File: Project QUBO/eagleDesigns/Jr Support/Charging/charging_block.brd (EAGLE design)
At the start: 160 x 100 mm, 115 parts

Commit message: 
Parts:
- removed U$38: (no value), resistor:DRQ125-600
- added L1, L2: 10u, resistor:L6100
- added LED7, LED8: Green, led:CHIP-LED0805
- added R28, R33: 330, resistor:R0805
- moved U$21 217.5 mm to (141.0, 17.8), turned to 180 degrees
- moved LED6 212.1 mm to (114.3, 26.7)
- moved LED5 208.6 mm to (119.4, 26.7)
- moved LED4 207.3 mm to (124.5, 26.7)
- moved U$2 194.7 mm to (97.8, 54.0), turned to 180 degrees
- moved C12 187.0 mm to (87.6, 20.3)
- moved U$20 185.2 mm to (115.6, 90.2)
- moved R22 176.3 mm to (109.2, 24.1)
- moved U$5 175.7 mm to (95.2, 63.5)
- moved U$19 174.4 mm to (123.2, 90.2)
- moved R21 170.3 mm to (109.2, 27.9)
- moved D2 169.9 mm to (83.9, 52.9), turned to 270 degrees
- moved R18 166.0 mm to (118.1, 22.9)
- moved R16 165.1 mm to (125.7, 33.0)
- moved R20 164.3 mm to (109.2, 31.8)
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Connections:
- new net N$35: LED7.A, R28.1
- new net N$57: LED8.A, R33.1
- net GND: now also LED7.C, LED8.C
- net N$17: now also L2.P$1; no longer U$38.P$2
- net N$20: now also L2.P$2; no longer U$38.P$4
- net N$77: now also L1.P$2; no longer U$38.P$3
- net N$81: now also L1.P$1; no longer U$38.P$1
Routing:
- net GND: track 0.00 -> 2.36 mm, vias 0 -> 1

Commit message: Charging board layout, rev. 1
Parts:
- added R35, R36, R37: 0, resistor:R0805
- C19: value 100u,<50mO -> 120uF; device resistor:C0805 -> resistor:E3,5-8
- C84: value 100u,<50mO -> 120u; device resistor:C0805 -> resistor:E3,5-8
- R28: value 330 -> 1.5k
- moved V_OUT 96.4 mm to (87.0, 88.3)
- moved U$21 82.9 mm to (87.0, 80.6)
- moved U$19 74.3 mm to (49.5, 80.6), flipped to the bottom, turned to 270 degrees
- moved ON 71.5 mm to (56.5, 34.9)
- moved U$58 71.4 mm to (62.2, 36.2), turned to 90 degrees
- moved C60 66.8 mm to (62.9, 45.1)
- moved R23 60.0 mm to (62.9, 42.5), turned to 180 degrees
- moved R24 57.7 mm to (62.9, 40.0), turned to 180 degrees
- moved U$56 57.3 mm to (62.2, 48.9)
- moved U$57 55.7 mm to (56.5, 44.5), turned to 270 degrees
- moved U$20 54.7 mm to (61.0, 86.4), turned to 180 degrees
- moved C61 53.4 mm to (54.6, 40.0)
- moved C62 52.7 mm to (59.7, 40.0), turned to 270 degrees
- moved AUDIO 52.3 mm to (26.7, 89.5), turned to 180 degrees
- moved R14 47.3 mm to (29.2, 83.2), turned to 270 degrees
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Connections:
- net N$11 renamed BATT1_P
- net N$15 renamed DLO_2
- net N$16 renamed DHI_2
- net N$17 renamed L-IN_2
- net N$18 renamed PGND_2
- net N$20 renamed CS_2
- net N$21 renamed THM_2
- net N$42 renamed DCIN_2
- net N$43 renamed BATT2_P
- net N$45 renamed VIN
- net N$46 renamed FET-G_1
- net N$56 renamed FET-D_1
- net N$77 renamed CS_1
- removed net N$48: C60.2, ON.P$2, U$56.P$3, U$58.P$1
- removed net V_BATT1: C83.1, C84.1, R29.1, R34.1, U$17.P$2, U$33.7
- removed net V_BATT2: C18.1, C19.1, R5.1, R7.1, U$1.7, U$18.P$2
- new net BATT1_M: BATT1_CHARGE.P$2, R35.1, R37.1, U$15.P$1, U$40.P$2
- new net BATT2_M: BATT2_CHARGE.P$2, R36.2, U$13.P$1, U$6.P$2
- new net BATT_1: C83.1, C84.+, R29.1, R34.1, U$17.P$2, U$33.7
- new net BATT_2: C18.1, C19.+, R5.1, R7.1, U$1.7, U$18.P$2
- net !SHDN!: now also R33.2
- net GND: now also C19.-, C60.2, C84.-, ON.P$2, R35.2, R36.1, R37.2, U$56.P$3, U$58.P$1; no longer BATT1_CHARGE.P$2, BATT2_CHARGE.P$2, C19.2, C84.2, U$13.P$1, U$15.P$1, U$40.P$2, U$6.P$2
- net V_SHORE: now also R28.2
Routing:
- net V_SHORE: track 0.00 -> 241.1 mm, vias 0 -> 5
- net !SHDN!: track 0.00 -> 58.3 mm, vias 0 -> 4
- net BATT_2: track 0.00 -> 41.8 mm
- net N$31: track 0.00 -> 36.5 mm, vias 0 -> 2
- net N$27: track 0.00 -> 29.9 mm, vias 0 -> 2
- net THM_2: track 0.00 -> 27.8 mm, vias 0 -> 1
- net N$32: track 0.00 -> 27.2 mm, vias 0 -> 2
- net N$38: track 0.00 -> 25.5 mm, vias 0 -> 2
- net N$24: track 0.00 -> 23.7 mm, vias 0 -> 2
- net VIN: track 0.00 -> 23.7 mm
- net CS_1: track 0.00 -> 23.1 mm, vias 0 -> 2
- net N$55: track 0.00 -> 20.4 mm
- net GND: track 2.36 -> 22.4 mm
- net BATT_1: track 0.00 -> 19.0 mm, vias 0 -> 2
- net N$54: track 0.00 -> 18.9 mm
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- added copper zone on layer 1, net BATT1_M
- added copper zone on layer 1, net BATT1_P
- added copper zone on layer 1, net BATT2_M
- added copper zone on layer 1, net BATT2_P
- added copper zone on layer 1, net BATT_1
- added copper zone on layer 1, net CS_2
- added copper zone on layer 1, net FET-D_1
- added copper zone on layer 1, net GND
- added copper zone on layer 16, net L-IN_2
- added copper zone on layer 16, net N$81
- removed copper zone on layer 16, net GND
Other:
- board size 160 x 100 mm -> 85.1 x 77.1 mm

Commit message: Charging board version 1 - completed
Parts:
- removed U$22: GPTS203212B, switches:GPTS203211B
- added BATT1_SWITCH: GPTS203212B, switches:GPTS203211B
- B1-HFET, U$2, U$3, U$37: value (none) -> FDMC8360LET40PWR33
- L1, L2: value 10u -> 10uH
- LED1, LED4: value Green -> FASTCHG
- LED2, LED5: value Green -> FULLCHG
- LED3, LED6: value Red -> FAULT
- LED7: value Green -> Shore Power
- LED8: value Green -> CHARGING
- moved LED1 4.44 mm to (23.5, 69.2), turned to 180 degrees
- moved LED2 2.54 mm to (23.5, 75.6), turned to 180 degrees
- moved R11 1.27 mm to (25.4, 76.8)
- moved R9 1.27 mm to (25.4, 72.4)
- renumbered AUDIO to BUZZER, AUDIO1 to BUZZER2, BATT1_CHARGE to BATT1_IN, BATT2_CHARGE to BATT2_IN, ON to CHARGING-SWITCH, U$13 to 24V-TVS_3, U$15 to 24V-TVS_2, U$17 to BATT1_FUSE, U$18 to BATT2_FUSE, U$20 to INPUT-SWITCH, U$21 to 24V-TVS_OUT, U$24 to BATT2_SWITCH, U$33 to BATT1_IC, U$34 to B1-HFET, U$39 to B1-ZENER, U$4 to 24V-TVS_1, U$58 to 5V-TVS_1, VIN to SHORE_IN, V_OUT to SHORE_OUT
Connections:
- net GND: now also BATT1_SWITCH.P$1; no longer U$22.P$1
- net N$52: now also BATT1_SWITCH.P$2; no longer U$22.P$2
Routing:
- net V_SHORE: track 241.1 -> 185.9 mm
- net N$52: track 2.74 -> 13.7 mm
- net CS_1: track 23.1 -> 12.1 mm
- added copper zone on layer 1, net CS_1
- added copper zone on layer 16, net V_SHORE
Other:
- board text added: "Ben Hurwitz R@M 2017"

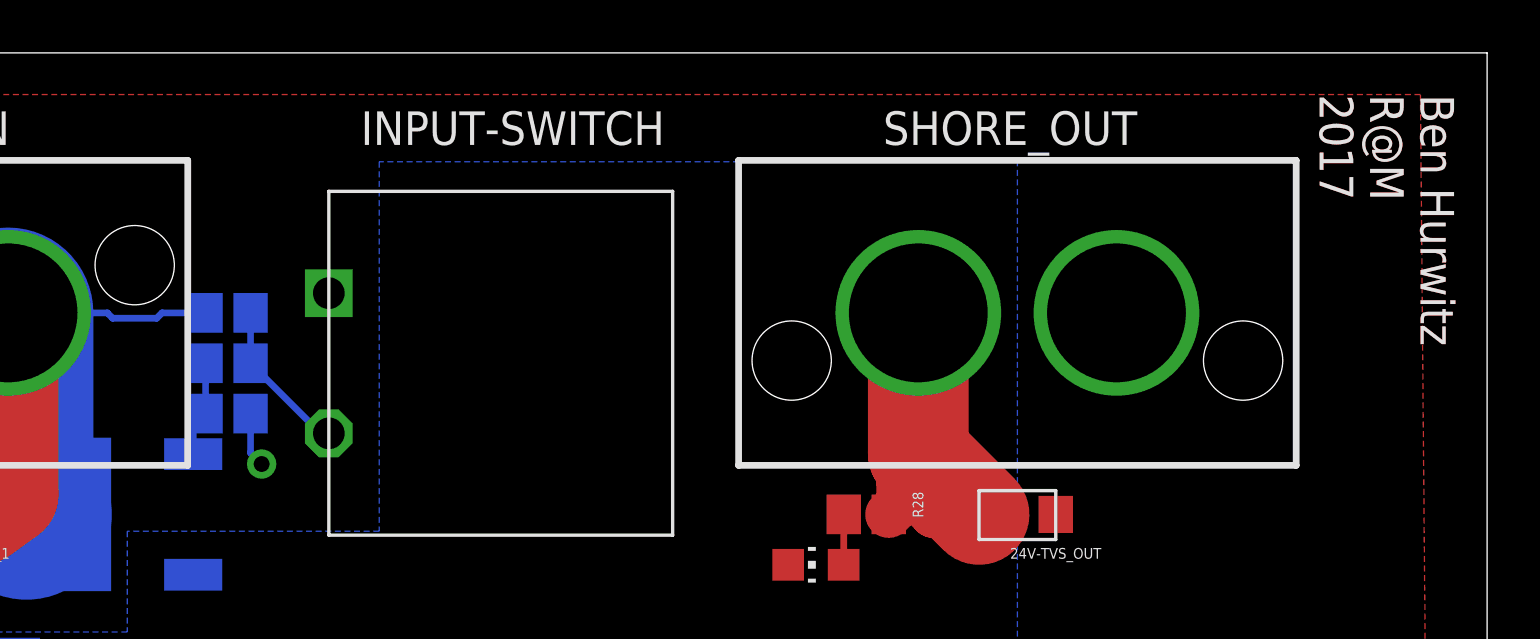
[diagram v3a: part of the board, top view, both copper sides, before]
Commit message: 
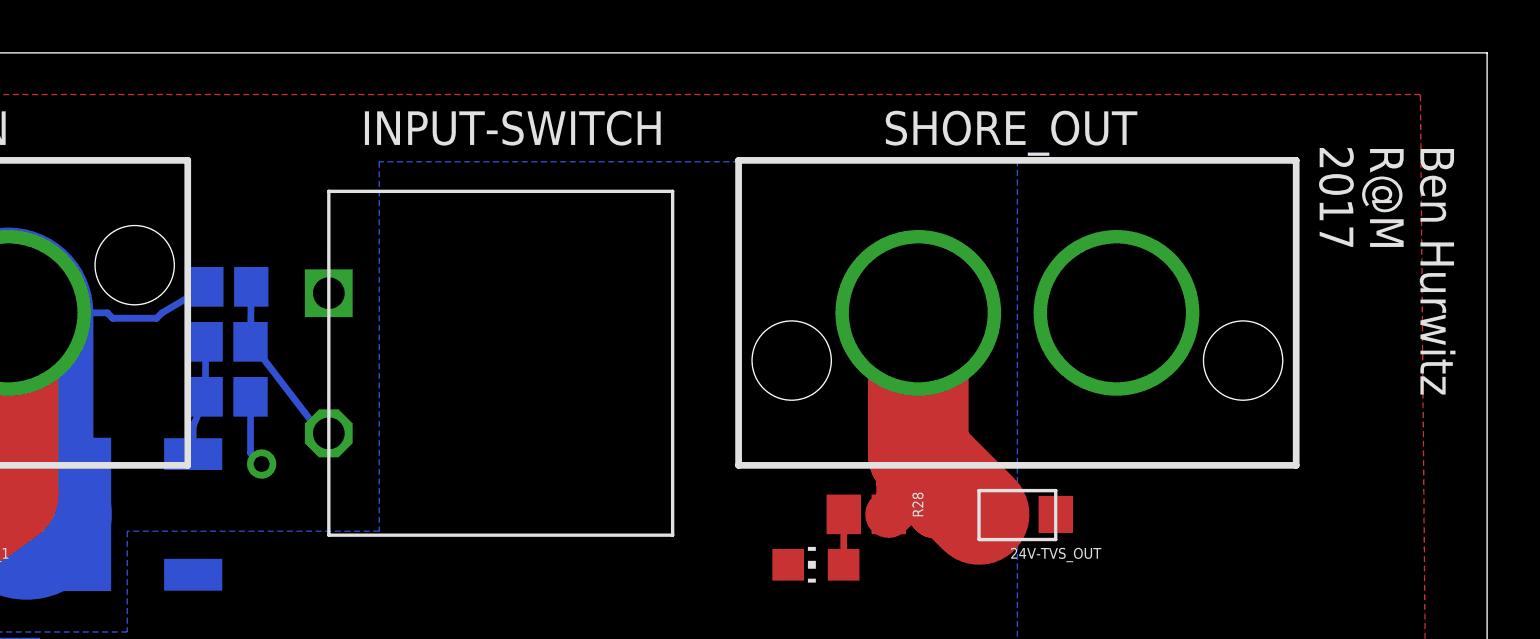
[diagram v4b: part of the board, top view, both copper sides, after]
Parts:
- moved R26 0.98 mm to (57.2, 89.2)
- moved R25 0.81 mm to (57.1, 87.2)
- moved C20 0.64 mm to (57.1, 85.1)
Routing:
- net N$51: track 5.96 -> 6.75 mm
- net N$47: track 3.63 -> 4.34 mm
- net GND: track 22.4 -> 23.0 mm
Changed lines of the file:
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@@
 <layer number="22" name="bPlace" color="7" fill="1" visible="yes" active="yes"/>
 <layer number="23" name="tOrigins" color="15" fill="1" visible="yes" active="yes"/>
-<layer number="24" name="bOrigins" color="15" fill="1" visible="no" active="yes"/>
+<layer number="24" name="bOrigins" color="15" fill="1" visible="yes" active="yes"/>
 <layer number="25" name="tNames" color="7" fill="1" visible="yes" active="yes"/>
 <layer number="26" name="bNames" color="7" fill="1" visible="yes" active="yes"/>
@@
 <wire x1="104.755" y1="98.095" x2="19.685" y2="98.095" width="0" layer="20"/>
 <wire x1="19.685" y1="98.095" x2="19.685" y2="20.955" width="0" layer="20"/>
-<text x="98.425" y="96.52" size="1.27" layer="1" ratio="7" rot="SR270">Ben Hurwitz
-R@M
-2017</text>
-<text x="98.425" y="96.52" size="1.27" layer="21" ratio="7" rot="SR270">Ben Hurwitz
+<text x="98.425" y="94.615" size="1.27" layer="21" ratio="15" rot="SR270">Ben Hurwitz
 R@M
 2017</text>
@@
 <attribute name="VALUE" x="72.555946875" y="68.7762" size="0.4064" layer="27" ratio="7" rot="R270"/>
 </element>
-<element name="C20" library="resistor" package="C0805" value="2.2u" x="57.15" y="84.455" smashed="yes" rot="MR180">
-<attribute name="NAME" x="58.801" y="84.709" size="0.4064" layer="26" ratio="7" rot="MR180"/>
-<attribute name="VALUE" x="55.499" y="84.074" size="0.4064" layer="28" ratio="7" rot="MR0"/>
+<element name="C20" library="resistor" package="C0805" value="2.2u" x="57.15" y="85.09" smashed="yes" rot="MR180">
+<attribute name="NAME" x="58.801" y="85.344" size="0.4064" layer="26" ratio="7" rot="MR180"/>
+<attribute name="VALUE" x="55.499" y="84.709" size="0.4064" layer="28" ratio="7" rot="MR0"/>
 </element>
 <element name="C3" library="resistor" package="C0805" value="2.2u" x="68.15321875" y="66.36519375" smashed="yes" rot="R180">
@@
 <element name="C73" library="resistor" package="C0805" value="47n" x="33.15330625" y="63.22415" smashed="yes" rot="R180">
 <attribute name="NAME" x="31.13685" y="63.88730625" size="0.4064" layer="25" ratio="7" rot="R270"/>
-<attribute name="VALUE" x="33.26769375" y="62.12485" size="0.4064" layer="27" ratio="7"/>
+<attribute name="VALUE" x="33.3270125" y="62.108671875" size="0.254" layer="27" ratio="7"/>
 </element>
 <element name="C74" library="resistor" package="C0805" value="1n" x="37.0474125" y="58.09889375" smashed="yes" rot="R270">
@@
 <attribute name="VALUE" x="64.389" y="40.767" size="0.4064" layer="27" ratio="7" rot="R270"/>
 </element>
-<element name="R25" library="resistor" package="R0805" value="43k" x="57.15" y="86.36" smashed="yes" rot="MR180">
-<attribute name="NAME" x="58.928" y="86.614" size="0.4064" layer="26" ratio="7" rot="MR180"/>
-<attribute name="VALUE" x="55.372" y="85.979" size="0.4064" layer="28" ratio="7" rot="MR0"/>
-</element>
-<element name="R26" library="resistor" package="R0805" value="4.3k" x="57.15" y="88.265" smashed="yes" rot="MR180">
-<attribute name="NAME" x="58.928" y="89.154" size="0.4064" layer="26" ratio="7" rot="MR180"/>
-<attribute name="VALUE" x="59.182" y="89.154" size="0.4064" layer="28" ratio="7" rot="MR0"/>
+<element name="R25" library="resistor" package="R0805" value="43k" x="57.15" y="87.169459375" smashed="yes" rot="MR180">
+<attribute name="NAME" x="58.928" y="87.423459375" size="0.4064" layer="26" ratio="7" rot="MR180"/>
+<attribute name="VALUE" x="55.372" y="86.788459375" size="0.4064" layer="28" ratio="7" rot="MR0"/>
+</element>
+<element name="R26" library="resistor" package="R0805" value="4.3k" x="57.176840625" y="89.24891875" smashed="yes" rot="MR180">
+<attribute name="NAME" x="58.954840625" y="90.13791875" size="0.4064" layer="26" ratio="7" rot="MR180"/>
+<attribute name="VALUE" x="59.208840625" y="90.13791875" size="0.4064" layer="28" ratio="7" rot="MR0"/>
 </element>
 <element name="R27" library="resistor" package="R0805" value="4.3k" x="76.2" y="38.735" smashed="yes">
@@
 <wire x1="35.152753125" y1="66.3575" x2="34.77378125" y2="66.736471875" width="0.254" layer="1"/>
 <wire x1="33.07865" y1="66.477671875" x2="32.30805" y2="65.707071875" width="0.254" layer="1"/>
-<wire x1="58" y1="84.455" x2="58" y2="82.97" width="0.254" layer="16"/>
+<wire x1="58" y1="85.09" x2="58" y2="82.97" width="0.254" layer="16"/>
 <wire x1="58" y1="82.97" x2="58.42" y2="82.55" width="0.254" layer="16"/>
 <via x="58.42" y="82.55" extent="1-16" drill="0.6"/>
@@
 <contactref element="B1-HFET" pad="SOURCE3"/>
 <contactref element="L1" pad="P$1"/>
-<polygon width="0.254" layer="16" spacing="0.254" isolate="0.3048" thermals="no">
+<polygon width="0.254" layer="16" spacing="0.254" isolate="0.3048" thermals="no" rank="2">
 <vertex x="46.99" y="69.215"/>
 <vertex x="50.165" y="69.215"/>
@@
 <wire x1="48.8315" y1="88.265" x2="48.8315" y2="81.3435" width="6.4516" layer="16"/>
 <wire x1="48.8315" y1="81.3435" x2="49.53" y2="80.645" width="6.4516" layer="16"/>
-<wire x1="56.3" y1="88.265" x2="54.6537625" y2="88.265" width="0.254" layer="16"/>
+<wire x1="56.326840625" y1="89.24891875" x2="54.6537625" y2="88.265" width="0.254" layer="16"/>
 <wire x1="54.6537625" y1="88.265" x2="54.4505625" y2="88.0618" width="0.254" layer="16"/>
 <wire x1="54.4505625" y1="88.0618" x2="52.7882375" y2="88.0618" width="0.254" layer="16"/>
@@
 <contactref element="U$19" pad="1"/>
 <wire x1="55.83" y1="82.925" x2="55.83" y2="83.985" width="0.254" layer="16"/>
-<wire x1="55.83" y1="83.985" x2="56.3" y2="84.455" width="0.254" layer="16"/>
-<wire x1="56.3" y1="84.455" x2="56.3" y2="86.36" width="0.254" layer="16"/>
+<wire x1="55.83" y1="83.985" x2="56.3" y2="85.09" width="0.254" layer="16"/>
+<wire x1="56.3" y1="85.09" x2="56.3" y2="87.169459375" width="0.254" layer="16"/>
 </signal>
 <signal name="N$51">
@@
 <contactref element="INPUT-SWITCH" pad="P$2"/>
 <contactref element="R26" pad="2"/>
-<wire x1="58" y1="86.36" x2="58" y2="88.265" width="0.254" layer="16"/>
+<wire x1="58" y1="87.169459375" x2="58.026840625" y2="89.24891875" width="0.254" layer="16"/>
 <wire x1="60.96" y1="83.71" x2="60.65" y2="83.71" width="0.254" layer="16"/>
-<wire x1="60.65" y1="83.71" x2="58" y2="86.36" width="0.254" layer="16"/>
+<wire x1="60.65" y1="83.71" x2="58" y2="87.169459375" width="0.254" layer="16"/>
 </signal>
 <signal name="BATT1_P">
